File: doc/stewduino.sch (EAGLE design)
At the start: 4 parts

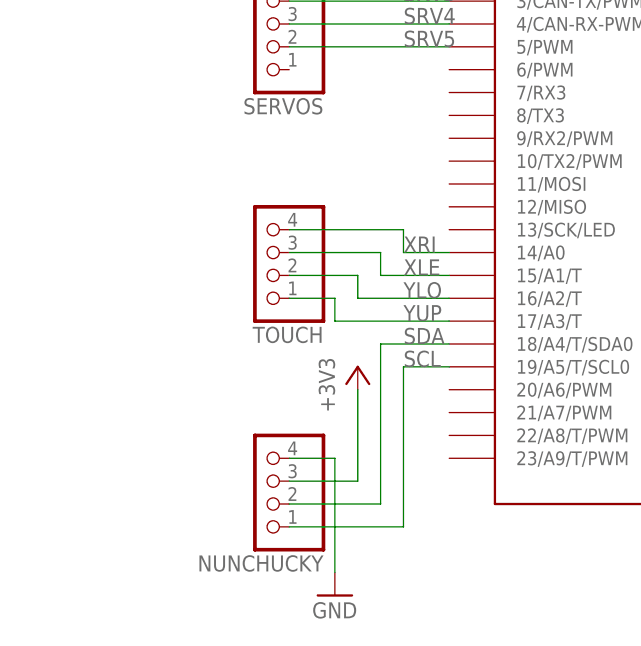
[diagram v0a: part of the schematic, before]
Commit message: FIXED: Stewduino wiring diagram / schematic shows Touchscreen connections on wrong analog pins.
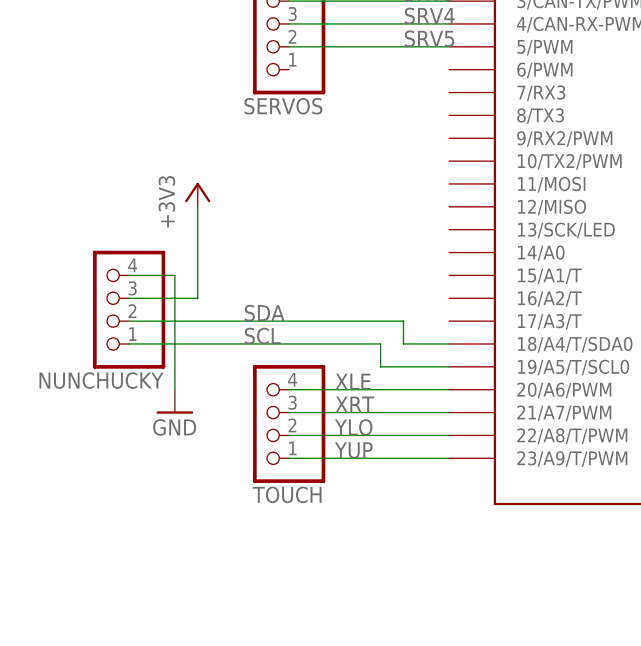
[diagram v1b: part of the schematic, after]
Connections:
- removed net XRI: TEENSY_3.2.14/A0, TOUCH.4
- new net XRT: TEENSY_3.2.21/A7/PWM, TOUCH.3
- net XLE: now also TEENSY_3.2.20/A6/PWM, TOUCH.4; no longer TEENSY_3.2.15/A1/T, TOUCH.3
- net YLO: now also TEENSY_3.2.22/A8/T/PWM; no longer TEENSY_3.2.16/A2/T
- net YUP: now also TEENSY_3.2.23/A9/T/PWM; no longer TEENSY_3.2.17/A3/T
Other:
- moved on the sheet: NUNCHUCKY, TOUCH
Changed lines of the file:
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@@
 <?xml version="1.0" encoding="utf-8"?>
 <!DOCTYPE eagle SYSTEM "eagle.dtd">
-<eagle version="7.3.0">
+<eagle version="8.5.0">
 <drawing>
 <settings>
 <setting alwaysvectorfont="no"/>
+<setting keepoldvectorfont="yes"/>
 <setting verticaltext="up"/>
 </settings>
@@
 <instance part="P+1" gate="VCC" x="93.98" y="93.98"/>
 <instance part="GND1" gate="1" x="93.98" y="10.16"/>
-<instance part="NUNCHUCKY" gate="A" x="17.78" y="15.24" rot="R180"/>
+<instance part="NUNCHUCKY" gate="A" x="0" y="35.56" rot="R180"/>
 <instance part="+3V1" gate="G$1" x="114.3" y="81.28"/>
-<instance part="+3V2" gate="G$1" x="27.94" y="27.94"/>
-<instance part="GND3" gate="1" x="25.4" y="2.54"/>
+<instance part="+3V2" gate="G$1" x="10.16" y="48.26"/>
+<instance part="GND3" gate="1" x="7.62" y="22.86"/>
 <instance part="SERVOS" gate="A" x="17.78" y="71.12" rot="R180"/>
-<instance part="TOUCH" gate="A" x="17.78" y="40.64" rot="R180"/>
+<instance part="TOUCH" gate="A" x="17.78" y="22.86" rot="R180"/>
 </instances>
 <busses>
@@
 <segment>
 <pinref part="NUNCHUCKY" gate="A" pin="4"/>
-<wire x1="20.32" y1="17.78" x2="25.4" y2="17.78" width="0.1524" layer="91"/>
-<wire x1="25.4" y1="17.78" x2="25.4" y2="5.08" width="0.1524" layer="91"/>
+<wire x1="2.54" y1="38.1" x2="7.62" y2="38.1" width="0.1524" layer="91"/>
+<wire x1="7.62" y1="38.1" x2="7.62" y2="25.4" width="0.1524" layer="91"/>
 <pinref part="GND3" gate="1" pin="GND"/>
 </segment>
@@
 <segment>
 <pinref part="TEENSY_3.2" gate="G$1" pin="18/A4/T/SDA0"/>
-<wire x1="38.1" y1="30.48" x2="30.48" y2="30.48" width="0.1524" layer="91"/>
-<wire x1="30.48" y1="30.48" x2="30.48" y2="12.7" width="0.1524" layer="91"/>
-<wire x1="30.48" y1="12.7" x2="20.32" y2="12.7" width="0.1524" layer="91"/>
+<wire x1="38.1" y1="30.48" x2="33.02" y2="30.48" width="0.1524" layer="91"/>
+<wire x1="33.02" y1="30.48" x2="33.02" y2="33.02" width="0.1524" layer="91"/>
+<wire x1="33.02" y1="33.02" x2="2.54" y2="33.02" width="0.1524" layer="91"/>
 <pinref part="NUNCHUCKY" gate="A" pin="2"/>
-<label x="33.02" y="30.48" size="1.778" layer="95"/>
+<label x="15.24" y="33.02" size="1.778" layer="95"/>
 </segment>
 </net>
@@
 <segment>
 <pinref part="TEENSY_3.2" gate="G$1" pin="19/A5/T/SCL0"/>
-<wire x1="38.1" y1="27.94" x2="33.02" y2="27.94" width="0.1524" layer="91"/>
-<wire x1="33.02" y1="27.94" x2="33.02" y2="10.16" width="0.1524" layer="91"/>
-<wire x1="33.02" y1="10.16" x2="20.32" y2="10.16" width="0.1524" layer="91"/>
+<wire x1="38.1" y1="27.94" x2="30.48" y2="27.94" width="0.1524" layer="91"/>
+<wire x1="30.48" y1="27.94" x2="30.48" y2="30.48" width="0.1524" layer="91"/>
+<wire x1="30.48" y1="30.48" x2="2.54" y2="30.48" width="0.1524" layer="91"/>
 <pinref part="NUNCHUCKY" gate="A" pin="1"/>
-<label x="33.02" y="27.94" size="1.778" layer="95"/>
+<label x="15.24" y="30.48" size="1.778" layer="95"/>
 </segment>
 </net>
@@
 <segment>
 <pinref part="NUNCHUCKY" gate="A" pin="3"/>
-<wire x1="20.32" y1="15.24" x2="27.94" y2="15.24" width="0.1524" layer="91"/>
-<wire x1="27.94" y1="15.24" x2="27.94" y2="25.4" width="0.1524" layer="91"/>
+<wire x1="2.54" y1="35.56" x2="10.16" y2="35.56" width="0.1524" layer="91"/>
+<wire x1="10.16" y1="35.56" x2="10.16" y2="45.72" width="0.1524" layer="91"/>
 <pinref part="+3V2" gate="G$1" pin="+3V3"/>
 </segment>
@@
 </segment>
 </net>
-<net name="XRI" class="0">
-<segment>
-<pinref part="TEENSY_3.2" gate="G$1" pin="14/A0"/>
-<wire x1="38.1" y1="40.64" x2="33.02" y2="40.64" width="0.1524" layer="91"/>
-<wire x1="33.02" y1="40.64" x2="33.02" y2="43.18" width="0.1524" layer="91"/>
+<net name="XLE" class="0">
+<segment>
 <pinref part="TOUCH" gate="A" pin="4"/>
-<wire x1="33.02" y1="43.18" x2="20.32" y2="43.18" width="0.1524" layer="91"/>
-<label x="33.02" y="40.64" size="1.778" layer="95"/>
-</segment>
-</net>
-<net name="XLE" class="0">
-<segment>
-<pinref part="TEENSY_3.2" gate="G$1" pin="15/A1/T"/>
-<wire x1="38.1" y1="38.1" x2="30.48" y2="38.1" width="0.1524" layer="91"/>
-<wire x1="30.48" y1="38.1" x2="30.48" y2="40.64" width="0.1524" layer="91"/>
+<pinref part="TEENSY_3.2" gate="G$1" pin="20/A6/PWM"/>
+<wire x1="20.32" y1="25.4" x2="38.1" y2="25.4" width="0.1524" layer="91"/>
+<label x="25.4" y="25.4" size="1.778" layer="95"/>
+</segment>
+</net>
+<net name="XRT" class="0">
+<segment>
+<pinref part="TEENSY_3.2" gate="G$1" pin="21/A7/PWM"/>
 <pinref part="TOUCH" gate="A" pin="3"/>
-<wire x1="30.48" y1="40.64" x2="20.32" y2="40.64" width="0.1524" layer="91"/>
-<label x="33.02" y="38.1" size="1.778" layer="95"/>
+<wire x1="38.1" y1="22.86" x2="20.32" y2="22.86" width="0.1524" layer="91"/>
+<label x="25.4" y="22.86" size="1.778" layer="95"/>
 </segment>
 </net>
 <net name="YLO" class="0">
 <segment>
-<pinref part="TEENSY_3.2" gate="G$1" pin="16/A2/T"/>
-<wire x1="38.1" y1="35.56" x2="27.94" y2="35.56" width="0.1524" layer="91"/>
-<wire x1="27.94" y1="35.56" x2="27.94" y2="38.1" width="0.1524" layer="91"/>
+<pinref part="TEENSY_3.2" gate="G$1" pin="22/A8/T/PWM"/>
 <pinref part="TOUCH" gate="A" pin="2"/>
-<wire x1="27.94" y1="38.1" x2="20.32" y2="38.1" width="0.1524" layer="91"/>
-<label x="33.02" y="35.56" size="1.778" layer="95"/>
+<wire x1="38.1" y1="20.32" x2="20.32" y2="20.32" width="0.1524" layer="91"/>
+<label x="25.4" y="20.32" size="1.778" layer="95"/>
 </segment>
 </net>
 <net name="YUP" class="0">
 <segment>
-<pinref part="TEENSY_3.2" gate="G$1" pin="17/A3/T"/>
-<wire x1="38.1" y1="33.02" x2="25.4" y2="33.02" width="0.1524" layer="91"/>
-<wire x1="25.4" y1="33.02" x2="25.4" y2="35.56" width="0.1524" layer="91"/>
+<pinref part="TEENSY_3.2" gate="G$1" pin="23/A9/T/PWM"/>
 <pinref part="TOUCH" gate="A" pin="1"/>
-<wire x1="25.4" y1="35.56" x2="20.32" y2="35.56" width="0.1524" layer="91"/>
-<label x="33.02" y="33.02" size="1.778" layer="95"/>
-</segment>
-</net>
+<wire x1="38.1" y1="17.78" x2="20.32" y2="17.78" width="0.1524" layer="91"/>
+<label x="25.4" y="17.78" size="1.778" layer="95"/>
+</segment>
+</net>
